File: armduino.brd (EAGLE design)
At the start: 68.6 x 53.4 mm, 61 parts, among them IC1 78D2, IC3 LM1117-3.3V, Q1 12MHz, Q2 12MHz, T1 BC857, T2 BC857, U1 LPC11U35FBD48/401, U2 MKE02Z64VLD4, X1 POWERSUPPLY_DC21MMX, X2 USB-B_TH

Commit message: Version 0.4
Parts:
- removed C6: 100nF/25V, rcl:C0805K
- removed C7, C8: 33nF/25V, rcl:C0805K
- removed CONNECTED, RUNNING: (no value), led:CHIP-LED0805
- removed Q1: 12MHz, crystal:SM49
- removed R11: 120r, rcl:M0805
- removed T2: BC857, transistor:SOT23-BEC
- removed U$1: SWITCH-4X4, pessoal:SWITCH-4X4
- removed U1: LPC11U35FBD48/401, NXP_By_element14_Batch_1:QFP50P900X900X160-48N
- added C16, C19: 22pF, rcl:C0603K
- added C18: 2.2nF/16V, rcl:C0805K
- added C20: 1nF/25V, rcl:C0805K
- added CONNECTED1, RUNNING1: (no value), led:CHIP-LED0805
- added Q3: 8MHz, crystal:HC49/S
- added R20: 120r, rcl:M0805
- added U3: MKL26ZVFM4, freescale:QFN32
- C5: value 100nF/25V -> 1nF/25V
- IC1: value 78D2 -> 7805DT; device linear:D2PAK -> linear:TO252
- R10: value 120r -> 20k
- R14: value 2.2k -> 1k
- R18: value 24k -> 4.7k
- R19: value 39k -> 10k
- R4: value 1.5k -> 10k
- R5: value 10k -> 1M
- R7: value 10k -> 20k
- R8: value 2.2k -> 120r
- T1: value BC857 -> S9012; device transistor:SOT23-BEC -> transistor:SOT23-BCE
- moved R10 21.4 mm to (31.0, 43.3), turned to 0 degrees
- moved R4 16.8 mm to (33.0, 36.6), turned to 270 degrees
- moved R7 15.7 mm to (33.0, 32.0)
- moved R18 14.4 mm to (18.2, 22.9), turned to 0 degrees
- moved R5 13.0 mm to (21.7, 32.6)
- moved R19 11.9 mm to (23.1, 22.9), turned to 0 degrees
- moved R8 10.1 mm to (30.9, 23.7), turned to 270 degrees
- moved R14 7.45 mm to (10.5, 24.3)
- moved C5 7.20 mm to (24.0, 44.5), turned to 90 degrees
- moved T1 6.79 mm to (10.5, 27.7)
- moved D1 5.88 mm to (11.3, 13.9), turned to 180 degrees
- moved C2 4.07 mm to (14.4, 11.6)
- moved IC1 3.82 mm to (7.37, 19.2)
- moved R9 3.64 mm to (32.9, 40.5)
- moved C3 3.42 mm to (19.0, 14.8)
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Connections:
- removed net !USB_CON: R8.2, U1.22
- removed net LPC_RESET: ICSP1.5, R9.2, U1.3
- removed net LPC_SWCLK: ICSP1.1, U1.29
- removed net LPC_SWDIO: ICSP1.3, U1.39
- removed net N$10: C8.1, Q1.2, U1.7
- removed net N$15: R10.1, RUNNING.C
- removed net N$16: CONNECTED.C, R11.1
- removed net N$9: C7.1, Q1.1, U1.6
- removed net PROG_SWO: U1.1
- removed net USB_VBUS: FUSE1.2, R18.1, T2.C
- new net DEBUG_RESET: ICSP1.5, R18.2, R19.1, U3.19
- new net DEBUG_SWCLK: ICSP1.1, U3.10
- new net DEBUG_SWDIO: ICSP1.3, U3.13
- new net N$12: CONNECTED1.C, R20.1
- new net N$25: C16.1, Q3.2, R5.1, U3.18
- new net N$31: C18.1, U3.5
- new net USB_CON: FUSE1.2, R18.1, T1.E
- net +3V3: now also C20.1, U3.15, U3.7; no longer C6.1, R5.1, R7.1, R9.1, T1.C, U1.44, U1.8
- net +5V: now also T1.C, U3.6; no longer T2.E
- net GND: now also C16.2, C18.2, C19.2, C20.2, R19.2, R20.2, R7.2, R8.2, U3.16, U3.2, U3.8, U3.EXP; no longer C6.2, C7.2, C8.2, R11.2, R19.1, U$1.1, U1.41, U1.5
- net N$11: now also RUNNING1.C; no longer R7.2, T1.B
- net N$13: now also RUNNING1.A, U3.24; no longer RUNNING.A, U1.30
- net N$14: now also CONNECTED1.A, U3.22; no longer CONNECTED.A, U1.42
- net N$22: now also T1.B; no longer T2.B
- net N$24: now also C19.1, Q3.1, R5.2, U3.17; no longer R18.2, R19.2, U1.14
- net N$6: now also R10.1, R9.2, U3.31; no longer R5.2, U$1.2, U1.4
- net N$8: now also R4.2, R7.1, U3.27; no longer R4.1, T1.E
- net PROG_NRESET: now also U3.30; no longer U1.12
- net PROG_RX: now also R9.1; no longer U1.46
- net PROG_SWCLK: now also U3.26; no longer U1.2
- net PROG_SWDIO: now also R4.1, U3.28; no longer U1.13
- net PROG_TX: now also U3.32; no longer U1.47
- net USB_D+: now also U3.3; no longer R4.2, U1.20
- net USB_D-: now also U3.4; no longer U1.19
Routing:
- net +5V: track 115.4 -> 165.2 mm, vias 1 -> 4
- net DEBUG_RESET: track 0.00 -> 47.1 mm, vias 0 -> 2
- net USB_VBUS: track 39.7 -> 0.00 mm, vias 2 -> 0
- net +3V3: track 178.1 -> 138.7 mm
- net PROG_NRESET: track 84.8 -> 123.1 mm
- net LPC_RESET: track 38.2 -> 0.00 mm, vias 1 -> 0
- net LPC_SWDIO: track 24.0 -> 0.00 mm, vias 1 -> 0
- net USB_CON: track 0.00 -> 23.2 mm, vias 0 -> 2
- net N$6: track 27.9 -> 7.55 mm
- net LPC_SWCLK: track 19.5 -> 0.00 mm, vias 1 -> 0
- net N$24: track 30.7 -> 11.8 mm, vias 2 -> 0
- net N$9: track 18.7 -> 0.00 mm
- net PROG_SWDIO: track 33.2 -> 17.7 mm, vias 2 -> 0
- net DEBUG_SWDIO: track 0.00 -> 13.0 mm
- net N$25: track 0.00 -> 11.7 mm
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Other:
- board text added: "ARMduino v. 0.4 REV 0"
- board text removed: "ARMduino v. 0.2 REV 0"
- board text removed: "D.Cuartielles"
- board text removed: "D.Mellis"
- board text removed: "G.Martino"
- board text removed: "M.Banzi"
- board text removed: "T.Igoe"

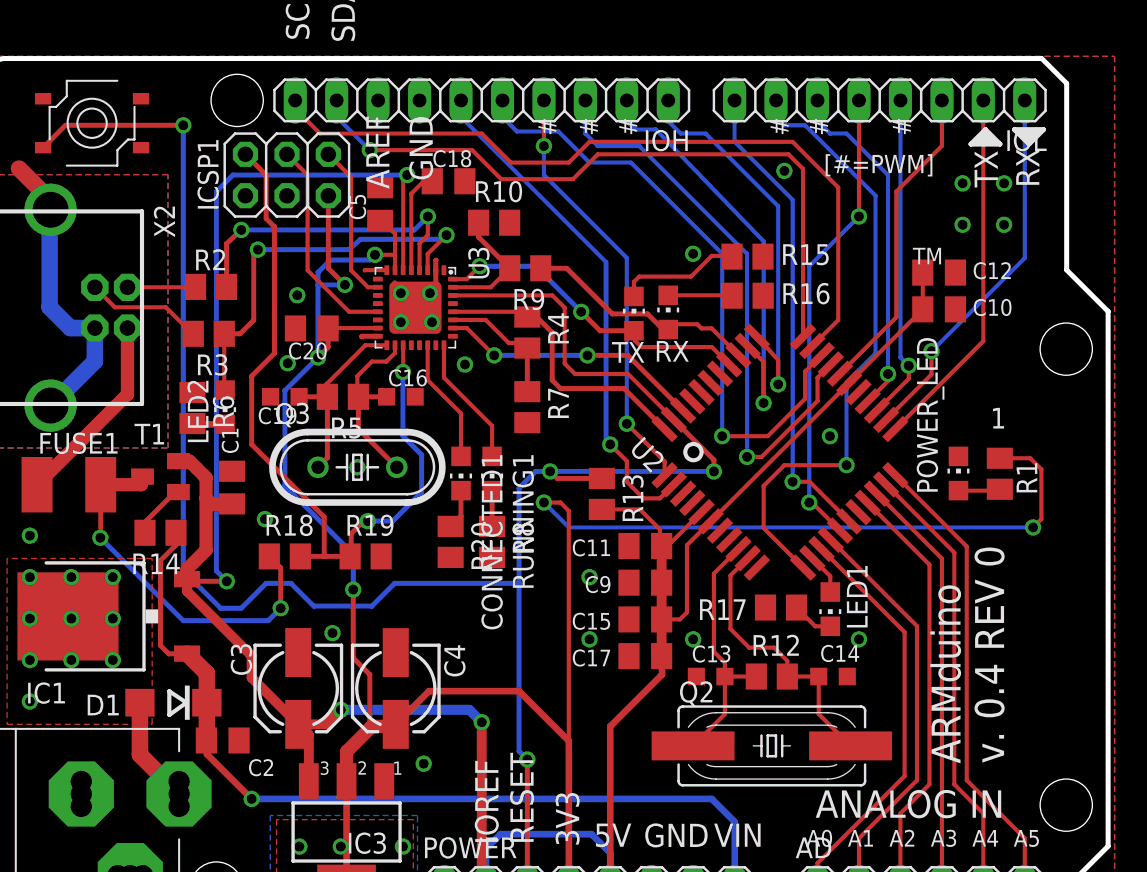
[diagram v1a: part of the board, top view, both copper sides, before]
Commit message: Removed PWM 3 and 5 from FTM0_FLT pins.
Some pins were moved around to fit PWM on FTM_CHx pins.
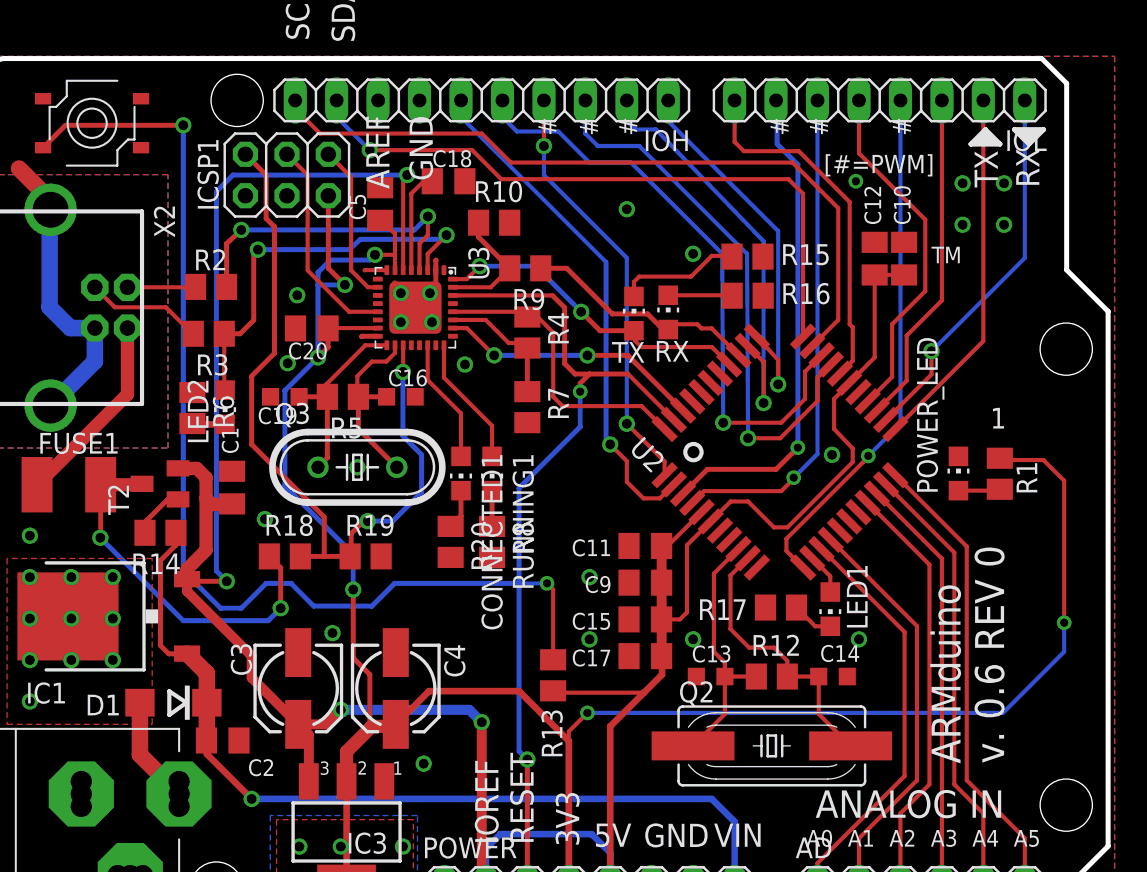
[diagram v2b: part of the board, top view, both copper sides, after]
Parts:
- removed T1: S9012, transistor:SOT23-BCE
- added T2: BC846, transistor:SOT23-BEC
- R14: value 1k -> 2.2k
- moved R13 11.5 mm to (34.6, 15.6)
- moved C12 4.04 mm to (54.3, 41.1), turned to 90 degrees
- moved C10 3.77 mm to (56.1, 41.1), turned to 90 degrees
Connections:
- net +5V: now also T2.E; no longer T1.C
- net N$22: now also T2.B; no longer T1.B
- net UC_IO_2: now also U2.25; no longer U2.29
- net UC_IO_4: now also U2.26; no longer U2.16
- net UC_IO_7: now also U2.29; no longer U2.17
- net UC_PWM_3: now also U2.12; no longer U2.25
- net UC_PWM_5: now also U2.4; no longer U2.26
- net UC_PWM_6: now also U2.3; no longer U2.12
- net USB_CON: now also T2.C; no longer T1.E
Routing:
- net UC_PWM_3: track 20.0 -> 31.9 mm
- net UC_PWM_5: track 21.3 -> 30.6 mm
- net UC_PWM_6: track 38.0 -> 30.0 mm
- net UC_IO_7: track 29.3 -> 22.0 mm, vias 1 -> 0
- net UC_IO_4: track 28.5 -> 21.6 mm, vias 2 -> 0
- net +5V: track 165.2 -> 171.3 mm
- net +3V3: track 138.7 -> 133.6 mm
- net PROG_NRESET: track 123.1 -> 118.5 mm
- net UC_I2C_SDA: track 42.5 -> 40.3 mm
- net UC_I2C_SCL: track 47.2 -> 45.4 mm
- net UC_SPI_CS: track 35.7 -> 34.1 mm
- net UC_IO_2: track 19.3 -> 20.7 mm
- net UC_SPI_MISO: track 38.2 -> 37.0 mm
- net UC_PWM_8: track 24.5 -> 23.6 mm
- net PROG_SWDIO: track 17.7 -> 18.2 mm
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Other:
- board text added: "ARMduino v. 0.6 REV 0"
- board text removed: "ARMduino v. 0.4 REV 0"

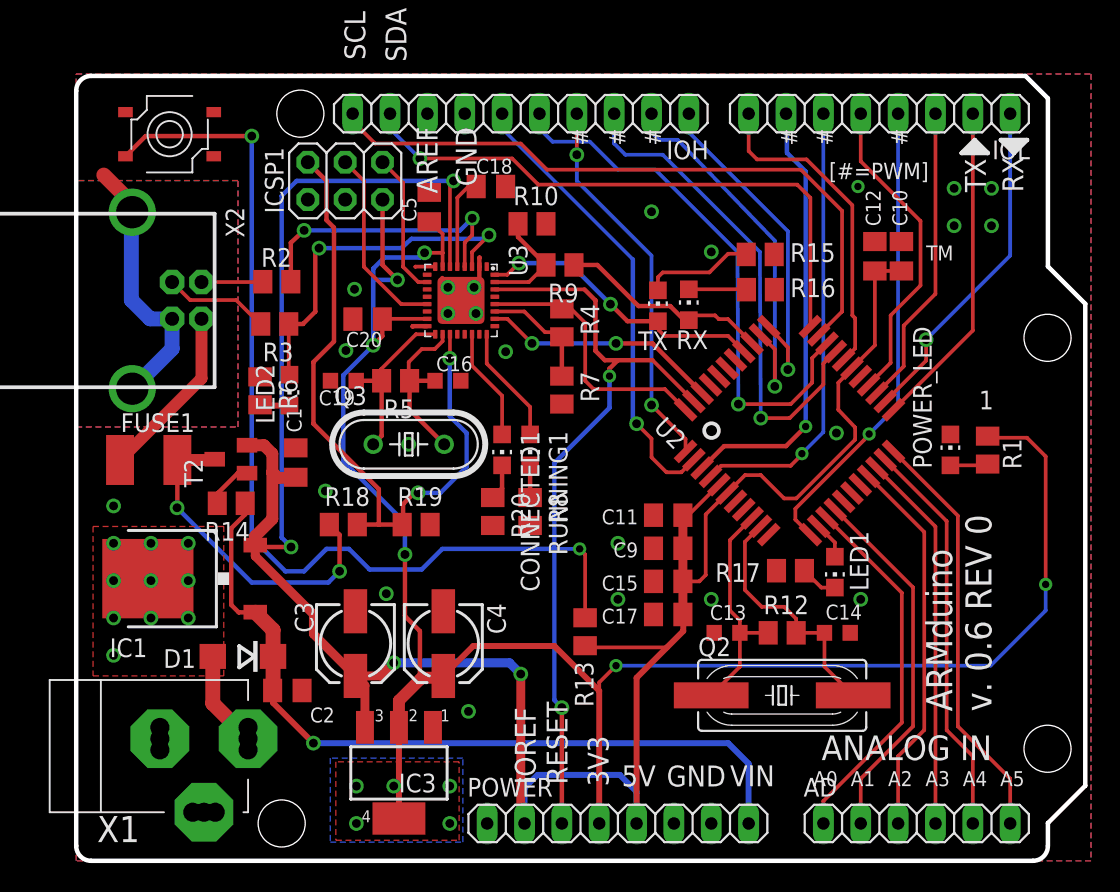
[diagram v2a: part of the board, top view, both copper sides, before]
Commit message: Correct voltage source selection, correct target XTAL.
 * Add LM358 to switch between external connector and USB source;
 * Target using 20MHz external crystal;
 * Re-route to fit new components;
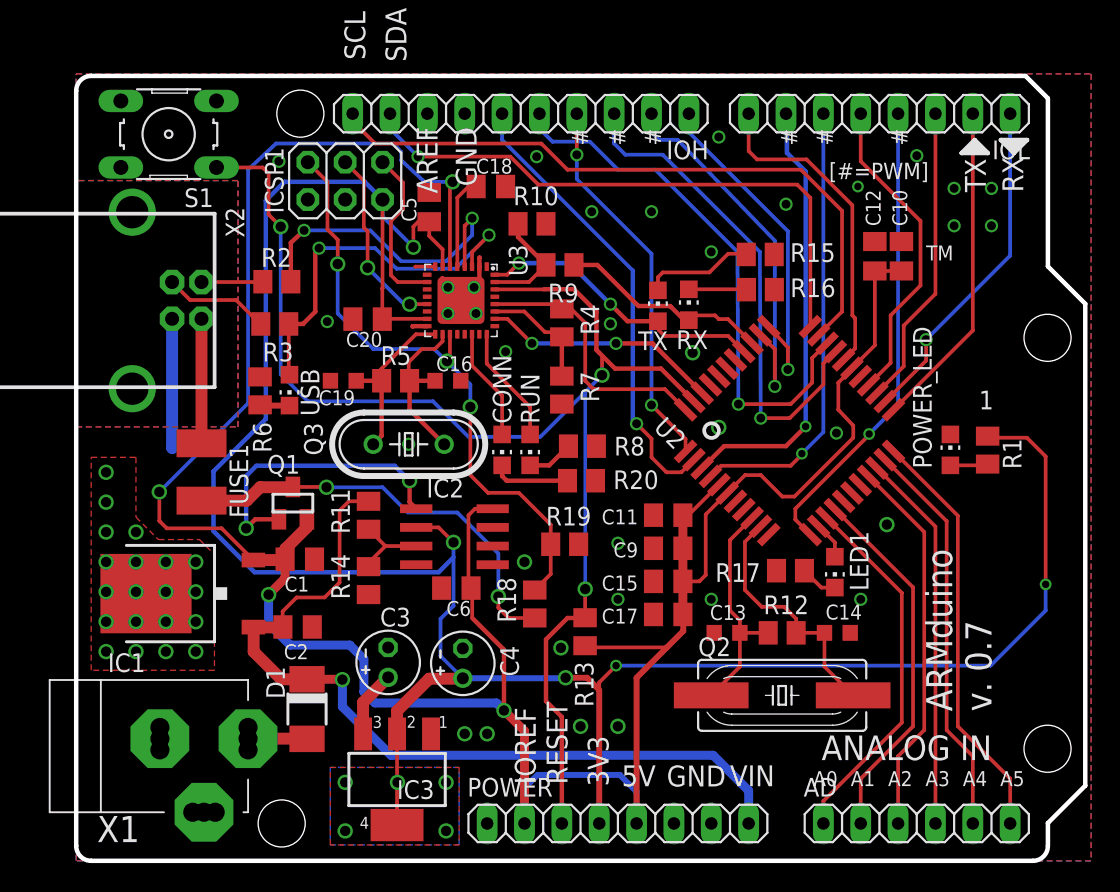
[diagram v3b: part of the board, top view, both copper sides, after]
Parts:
- removed RESET: SWITCH-4X4, pessoal:SWITCH-4X4
- removed T2: BC846, transistor:SOT23-BEC
- added C6: 100nF/50V, rcl:C0805K
- added IC2: LM358D, linear:SO08
- added Q1: FDN360P, transistor-power:SUPER-SOT3
- added R11: 10k, rcl:M0805
- added S1: (no value), switch-omron:B3F-10XX
- C3, C4: value 10uF/35V -> 10uF/16V; device rcl:153CLV-0505 -> rcl:E2-4
- D1: device diode:DO214AC -> diode:DO-214AC
- Q2: value 12MHz -> 20MHz
- R14: value 2.2k -> 10k
- moved R18 14.1 mm to (31.2, 17.5), turned to 90 degrees
- moved R14 10.7 mm to (19.9, 19.1), turned to 90 degrees
- moved R19 10.2 mm to (33.2, 21.5)
- moved C1 6.58 mm to (15.2, 20.5), turned to 0 degrees
- moved R20 6.39 mm to (34.4, 25.8), turned to 0 degrees
- moved R8 5.69 mm to (34.4, 28.2), turned to 0 degrees
- moved D1 5.64 mm to (15.7, 10.3), turned to 270 degrees
- moved C2 4.37 mm to (15.1, 15.9)
- moved FUSE1 3.68 mm to (8.52, 26.4), turned to 270 degrees
- moved C3 2.57 mm to (21.2, 13.5), turned to 90 degrees
- moved C4 1.88 mm to (26.3, 13.4), turned to 90 degrees
- moved IC1 1.02 mm to (7.25, 18.2)
- moved IC3 0.46 mm to (21.8, 5.53)
- renumbered CONNECTED1 to CONN, LED2 to USB, RUNNING1 to RUN
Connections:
- net N$12 renamed CONN
- removed net N$22: R14.2, T2.B
- new net N$15: IC2.3, R11.1, R14.2
- new net N$26: IC2.1, Q1.1
- new net N$9: C3.+, IC3.3
- net +3V3: now also IC2.2
- net +5V: now also C6.1, IC2.8, Q1.2; no longer C3.+, IC3.3, T2.E
- net GND: now also C6.2, IC2.4, IC2.5, IC2.6, R14.1, S1.3; no longer RESET.1, X2.P$1, X2.P$2
- net PROG_NRESET: now also S1.1; no longer RESET.2
- net USB_CON: now also Q1.3; no longer T2.C
- net VCC: now also R11.2; no longer R14.1
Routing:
- net +3V3: track 133.6 -> 165.1 mm, vias 11 -> 10
- net PROG_NRESET: track 118.5 -> 94.5 mm, vias 4 -> 3
- net N$26: track 0.00 -> 19.9 mm, vias 0 -> 2
- net +5V: track 171.3 -> 188.4 mm
- net GND: track 25.1 -> 15.4 mm, vias 34 -> 55
- net USB_CON: track 22.7 -> 28.9 mm
- net N$15: track 0.00 -> 5.59 mm
- net DEBUG_RESET: track 47.1 -> 41.9 mm, vias 2 -> 3
- net N$9: track 0.00 -> 4.55 mm
- net VCC: track 54.0 -> 57.4 mm
- net N$3: track 11.9 -> 8.46 mm
- net N$22: track 3.25 -> 0.00 mm
- net CONN: track 2.45 -> 5.31 mm
- net N$1: track 6.59 -> 4.01 mm
- net USB_D-: track 19.2 -> 21.6 mm
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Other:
- board text added: "ARMduino v. 0.7"
- board text removed: "ARMduino v. 0.6 REV 0"
